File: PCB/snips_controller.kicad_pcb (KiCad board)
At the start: 4 copper layers, 35 x 99.9 mm, 75 parts

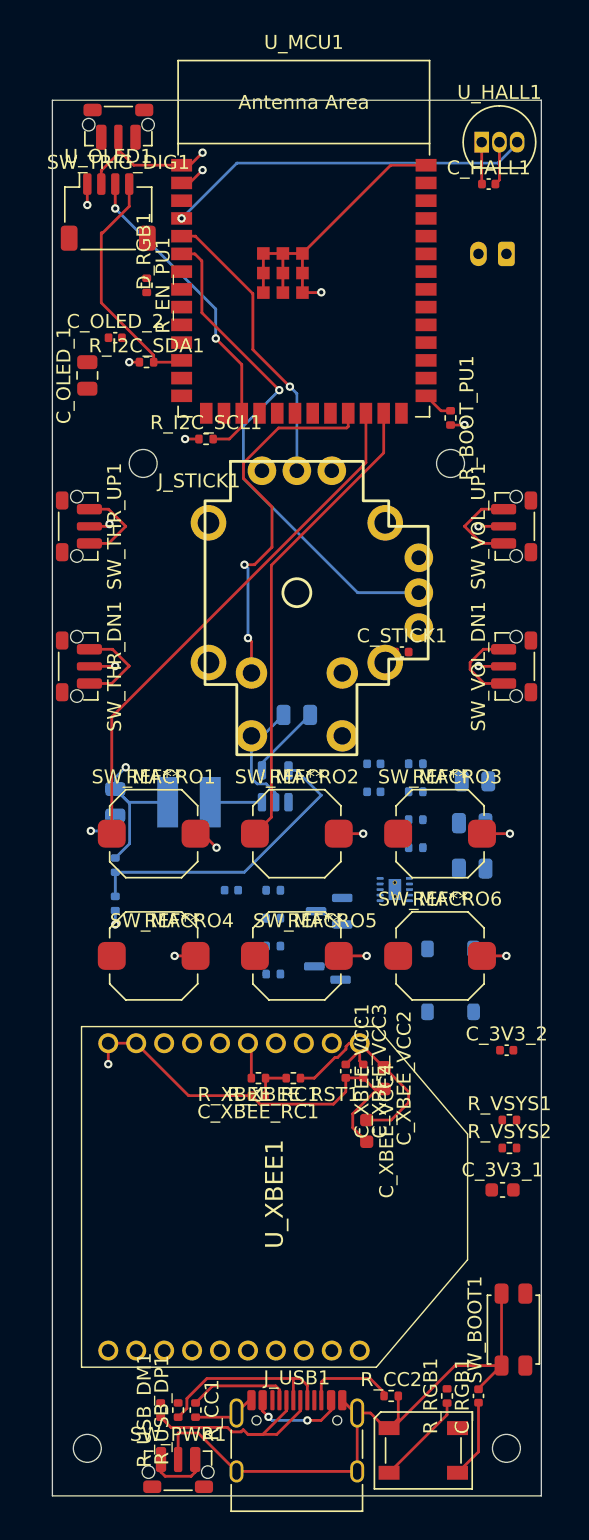
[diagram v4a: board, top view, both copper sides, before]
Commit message: task: board is fully routed
That was a pain, but it is all routed and connected now.
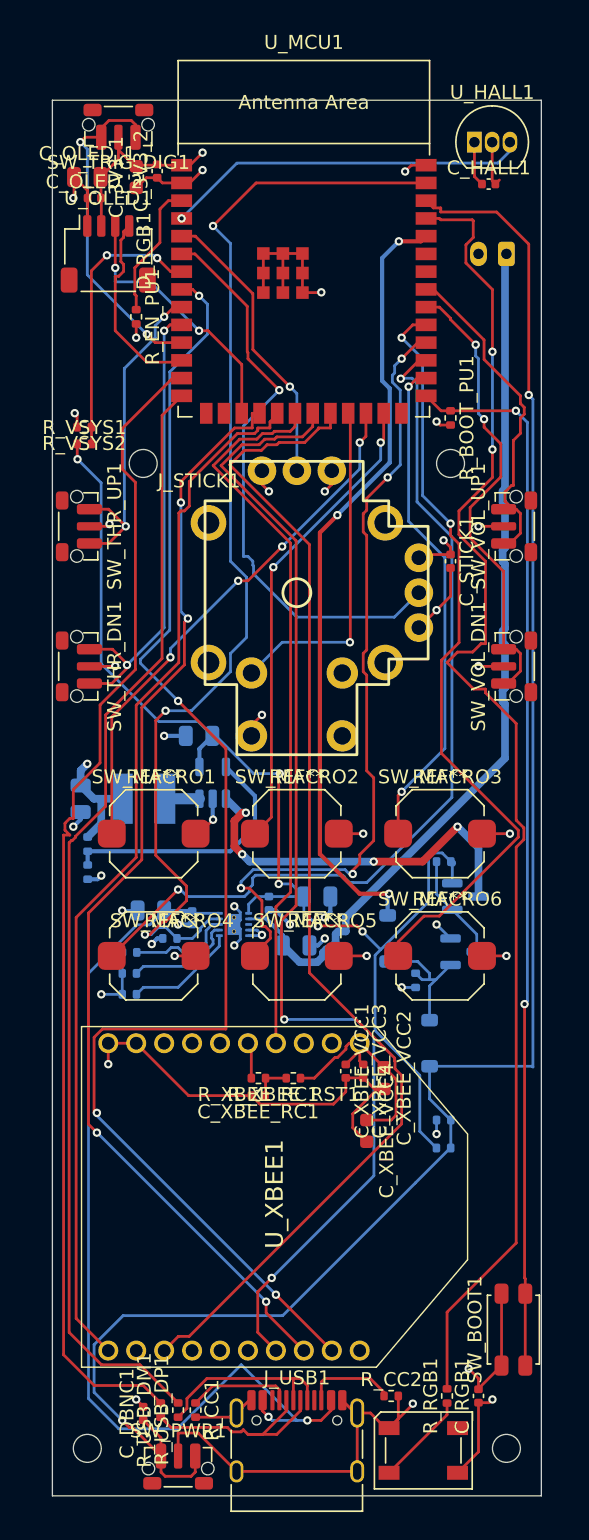
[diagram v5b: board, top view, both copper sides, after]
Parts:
- removed R_I2C_SCL1, R_I2C_SDA1: 4.7kΩ, Resistor_SMD:R_0402_1005Metric
- C_DBNC1: moved to F.Cu
- moved C_3V3_1 77.1 mm to (126.0, 65.5), turned to 90 degrees
- moved C_3V3_2 67.7 mm to (127.5, 65.1), turned to 90 degrees
- moved R_VSYS2 59.9 mm to (122.3, 83.4), turned to 180 degrees
- moved R_VSYS1 57.2 mm to (122.3, 84.6)
- moved C_DBNC1 38.0 mm to (126.5, 154.0), turned to 90 degrees
- moved R_ISET1 24.5 mm to (125.5, 121.0)
- moved R_TS1 24.0 mm to (125.5, 124.0)
- moved C_VIN_1 23.2 mm to (127.0, 118.0)
- moved R_VSET1 22.4 mm to (125.5, 122.5)
- moved R_BTN_PU1 22.1 mm to (148.0, 135.0), turned to 0 degrees
- moved R_STAT1 20.5 mm to (128.4, 120.0)
- moved C_BAT1 17.4 mm to (137.4, 120.5), turned to 0 degrees
- moved R_PWR_SENSE1 16.1 mm to (148.0, 133.0)
- moved C_VIN_2 15.8 mm to (130.0, 118.5), turned to -90 degrees
- moved C_OLED_1 14.2 mm to (122.5, 65.5), turned to 0 degrees
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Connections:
- U_MCU1 pad 10: /Buttons_Direct/BTN_VOL_DN -> /Buttons_Direct/BTN_THR_DN
- U_MCU1 pad 32: /Buttons_Direct/BTN_THR_UP -> /Buttons_Direct/BTN_VOL_DN
- U_MCU1 pad 33: /Buttons_Direct/BTN_THR_DN -> /Buttons_Direct/BTN_VOL_UP
- U_MCU1 pad 9: /Buttons_Direct/BTN_VOL_UP -> /Buttons_Direct/BTN_THR_UP
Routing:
- net /MCU_Core/PWR_BTN_SENSE: track 4.50 -> 130.8 mm, vias 0 -> 2
- net /MCU_Core/XBEE_SPI_ATTN: track 0.00 -> 97.8 mm, vias 0 -> 4
- net /MCU_Core/RGB_DIN: track 0.00 -> 96.9 mm, vias 0 -> 2
- net /MCU_Core/XBEE_ON_SLEEP: track 0.00 -> 85.4 mm
- net /MCU_Core/XBee_CS: track 0.00 -> 84.4 mm, vias 0 -> 2
- net /MCU_Core/USB_DM_MCU: track 0.00 -> 83.6 mm
- net /MCU_Core/STAT1: track 0.00 -> 81.0 mm, vias 0 -> 3
- net /MCU_Core/USB_DP_MCU: track 0.00 -> 80.3 mm
- net VSYS: track 5.40 -> 85.6 mm, vias 0 -> 5
- net /MCU_Core/SPI_SCK: track 0.00 -> 80.0 mm, vias 0 -> 4
- net /MCU_Core/SPI_MOSI: track 0.00 -> 75.4 mm
- net /MCU_Core/MCU_BOOT: track 2.19 -> 75.7 mm, vias 0 -> 2
- net /Buttons_Direct/BTN_MACRO4: track 0.00 -> 64.8 mm, vias 0 -> 2
- net VBAT: track 0.00 -> 63.9 mm
- net VBUS: track 6.97 -> 68.1 mm
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
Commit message: task: first validation pass
This is the results post first kicad-happy run.
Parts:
- added C_3V3_3: 39pF, Capacitor_SMD:C_0402_1005Metric, F.Cu at (127.3, 67.2)
- added D_VBUS_TVS1: PESD5V0S1BA, Diode_SMD:D_SOD-323, B.Cu at (137.4, 156.2)
- added REF**: Fiducial_1mm_Mask2mm, Fiducial:Fiducial_1mm_Mask2mm, F.Cu at (124.2, 78.3)
- added REF**: Fiducial_1mm_Mask2mm, Fiducial:Fiducial_1mm_Mask2mm, F.Cu at (151.3, 127.3)
- added REF**: Fiducial_1mm_Mask2mm, Fiducial:Fiducial_1mm_Mask2mm, F.Cu at (147.0, 150.1)
- added REF**: Fiducial_1mm_Mask2mm, Fiducial:Fiducial_1mm_Mask2mm, B.Cu at (150.4, 105.2)
- added REF**: Fiducial_1mm_Mask2mm, Fiducial:Fiducial_1mm_Mask2mm, B.Cu at (125.9, 95.3)
- added REF**: Fiducial_1mm_Mask2mm, Fiducial:Fiducial_1mm_Mask2mm, B.Cu at (122.8, 75.7)
- R_FB1: value 100kΩ -> 255kΩ
- moved SW_BOOT1 0.51 mm to (152.5, 148.1)
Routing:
- net /MCU_Core/XBEE_ON_SLEEP: track 85.4 -> 92.5 mm, vias 0 -> 2
- net /MCU_Core/SPI_SCK: track 80.0 -> 85.5 mm, vias 4 -> 0
- net GND: track 160.0 -> 165.4 mm, vias 36 -> 37
- net /MCU_Core/XBEE_SPI_ATTN: track 97.8 -> 101.2 mm
- net VBUS: track 68.1 -> 70.4 mm
- net 3V3: track 55.0 -> 56.0 mm
- net /Hall_Trigger/TRIG_ANALOG: track 26.1 -> 26.7 mm
- net /MCU_Core/SPI_MOSI: track 75.4 -> 74.9 mm, vias 0 -> 2

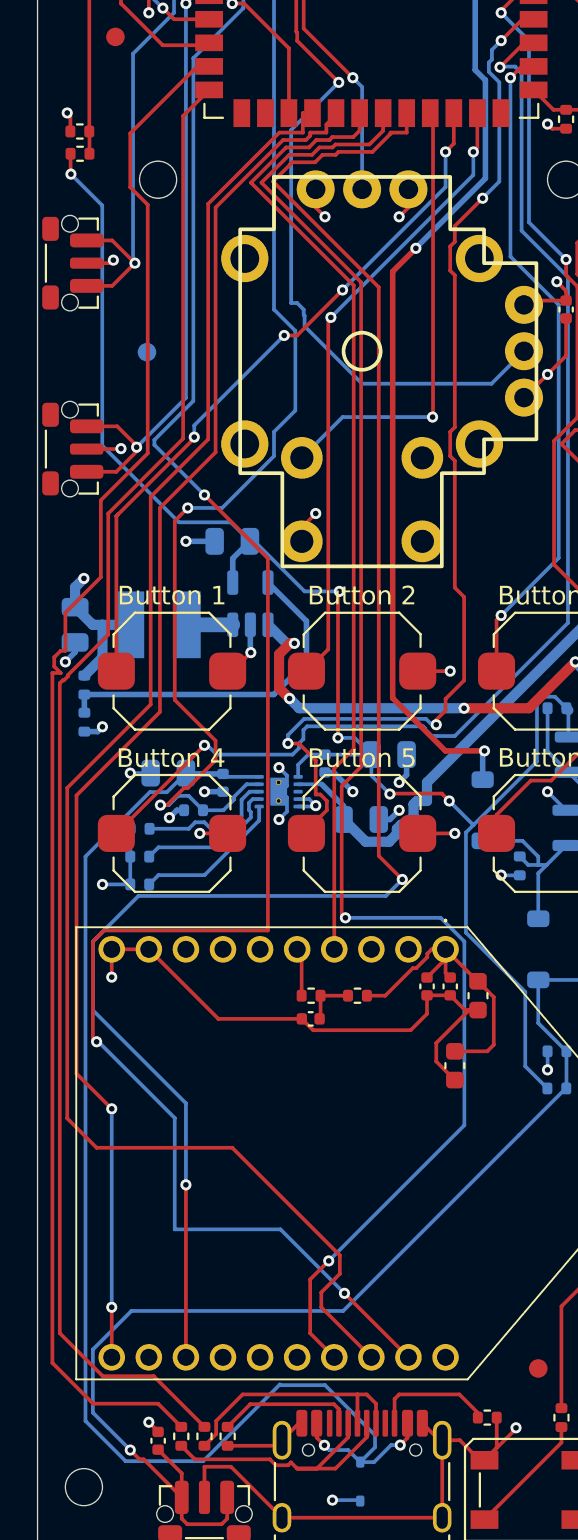
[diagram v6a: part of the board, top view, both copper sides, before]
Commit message: task: part number populated (#26)
kicad-happy run part 2 - MPN numbers populated
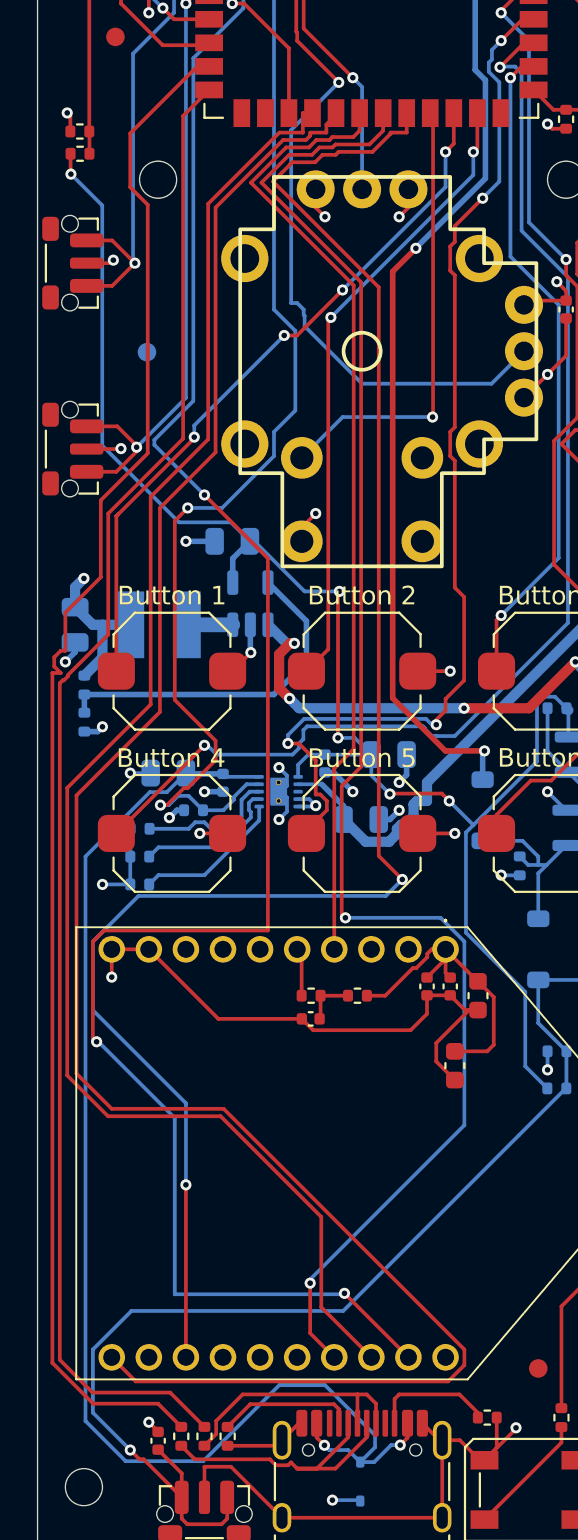
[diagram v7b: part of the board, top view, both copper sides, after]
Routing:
- net /MCU_Core/SPI_MOSI: track 74.9 -> 106.7 mm, vias 2 -> 0
- net /MCU_Core/XBEE_SPI_ATTN: track 101.2 -> 103.3 mm
- net /MCU_Core/SPI_SCK: track 85.5 -> 84.0 mm
- net /MCU_Core/USB_DP_MCU: track 80.3 -> 81.1 mm

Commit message: task: generate production files
We have wrapped up board validation. Gerbers are now generated. Logo generated. Good to go.
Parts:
- added G***: LOGO, LOGO, B.Cu at (133.9, 138.3)
- added G***: LOGO, LOGO, B.Cu at (146.5, 142.8)
- added G***: LOGO, R2Builders:R2Builders, B.Cu at (147.2, 155.8)
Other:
- board text added: "Snips Controllers V1.0 by @thePunderWoman github.com/thePunderWoman/SnipsControllers"
